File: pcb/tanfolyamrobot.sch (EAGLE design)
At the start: 78 parts, among them IC1 STM32F10XRXT6, IC2 7805, IC4 FT232RL, IC5 LD117AS33TR, M1 DRV8833, Q2 BSS123, Q3 BSS123, Q4 BSS123, X2 PWR, X6 KUSBVX-BS1N

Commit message: small schematic fixes #1
added notes
added component values/types
made RESET and BOOT0 circuit nicer
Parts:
- C10: value (none) -> 22u
- C11: value (none) -> 330n
- C12: value (none) -> 100n
- C13: value 1u -> 100n
- C14: value 2u2 -> 10u
- C16: value (none) -> 68u
- C17: value 22n? -> 22n
- C5, C6: value ? -> 15p
- D7: value (none) -> BAS85
- Q1: value (none) -> 16MHz
- R20, R21: value (none) -> 10K
- R22, R23: value (none) -> 20K
- R24, R25: value (none) -> 4K7
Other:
- note added: "Button's pin is pulled up internally"
- note added: "Check if backlight resistor is required for the used module"
- note added: "Solder jumpers for connecting FTDI output pins to the RESET and BOOT0 circuitry"
- note removed: "TODO: Backlight LED resistor value"
- note removed: "TODO: values, XTAL package"
- moved on the sheet: C10, C11, C12, C13, C14, C17, D3, D4, D5, D6, IC1RESET, JP10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

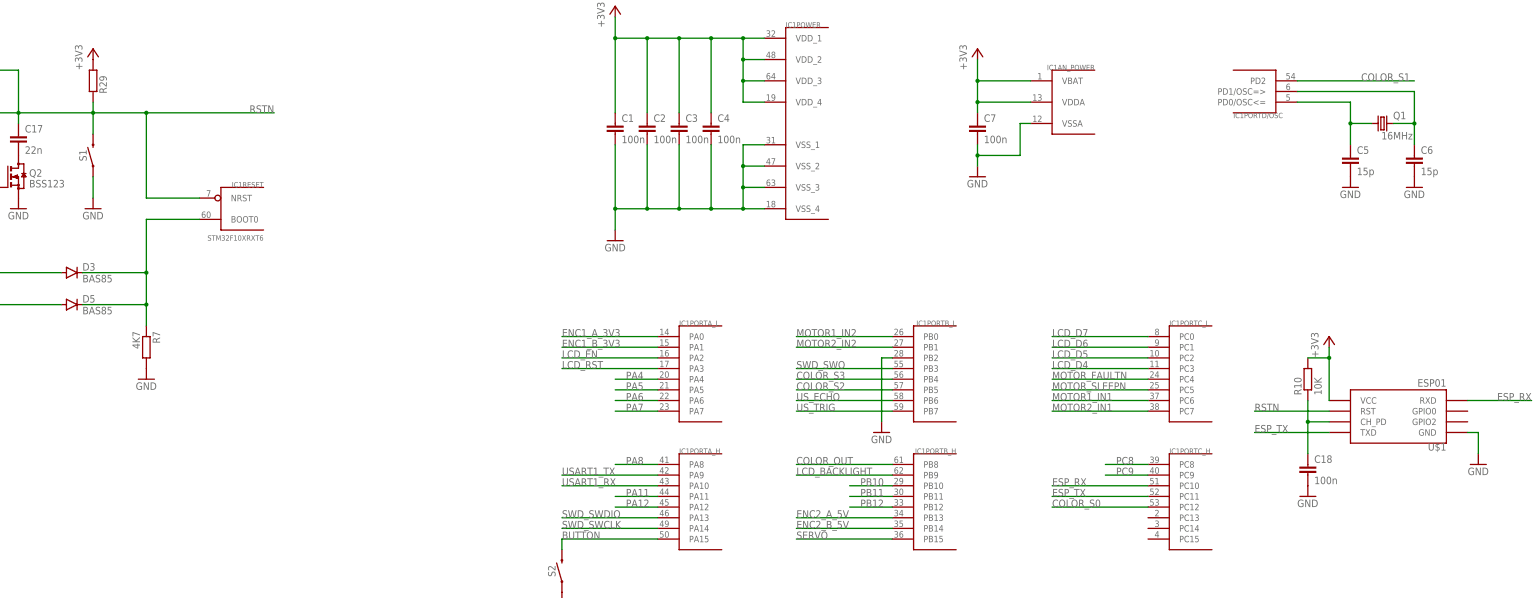
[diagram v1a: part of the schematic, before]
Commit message: added 100n cap to NRST (#1)
and also added ESP reset description
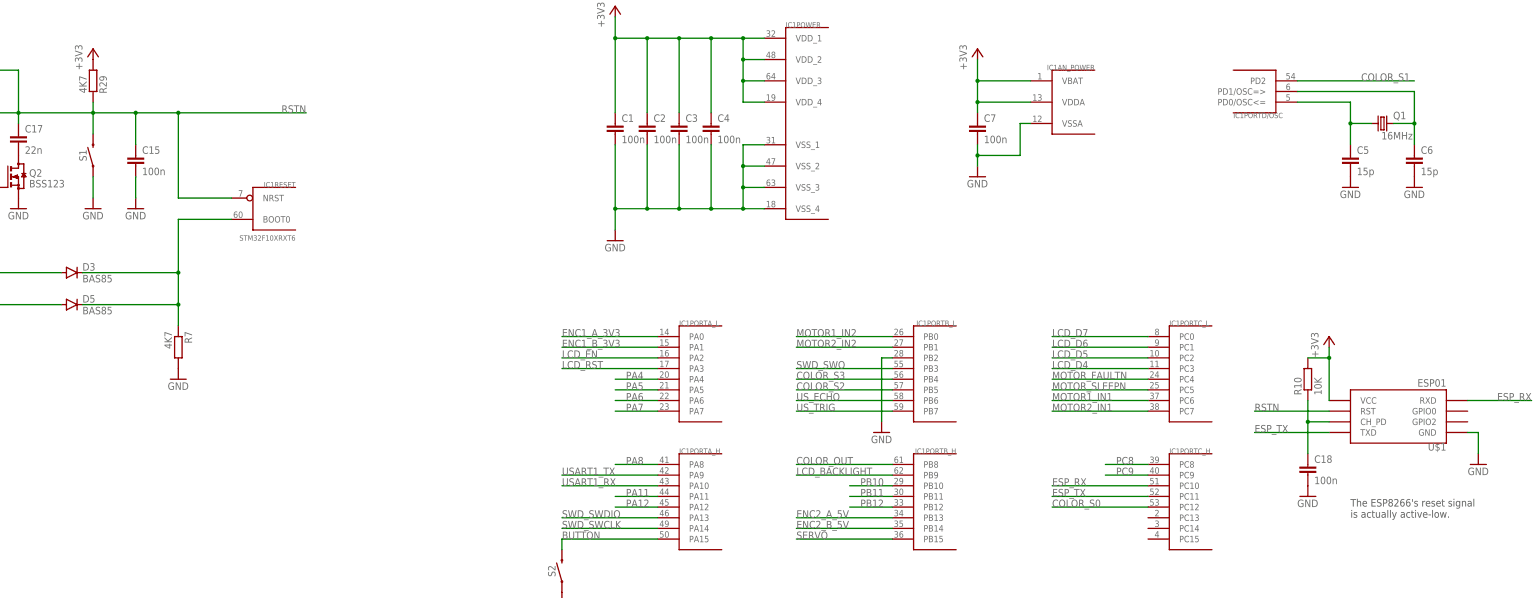
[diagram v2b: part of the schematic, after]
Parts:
- added C15: 100n, rcl:C-EUC0603
- R29: value (none) -> 4K7
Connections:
- net GND: now also C15.2
- net RSTN: now also C15.1
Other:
- note added: "The ESP8266's reset signal is actually active-low."
- moved on the sheet: IC1RESET, R7
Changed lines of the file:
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@@
 <part name="X6" library="con-kycon" library_urn="urn:adsk.eagle:library:157" deviceset="KUSBVX-BS1N" device="" package3d_urn="urn:adsk.eagle:package:7681/1"/>
 <part name="P+9" library="supply1" library_urn="urn:adsk.eagle:library:371" deviceset="+5V" device=""/>
-<part name="R29" library="rcl" library_urn="urn:adsk.eagle:library:334" deviceset="R-EU_" device="R0603" package3d_urn="urn:adsk.eagle:package:23555/3"/>
+<part name="R29" library="rcl" library_urn="urn:adsk.eagle:library:334" deviceset="R-EU_" device="R0603" package3d_urn="urn:adsk.eagle:package:23555/3" value="4K7"/>
 <part name="+3V11" library="supply1" library_urn="urn:adsk.eagle:library:371" deviceset="+3V3" device=""/>
 <part name="D3" library="diode" library_urn="urn:adsk.eagle:library:210" deviceset="DIODE-" device="MICROMELF-W" package3d_urn="urn:adsk.eagle:package:43441/2" value="BAS85"/>
@@
 <part name="GND31" library="supply1" library_urn="urn:adsk.eagle:library:371" deviceset="GND" device=""/>
 <part name="GND32" library="supply1" library_urn="urn:adsk.eagle:library:371" deviceset="GND" device=""/>
+<part name="C15" library="rcl" library_urn="urn:adsk.eagle:library:334" deviceset="C-EU" device="C0603" package3d_urn="urn:adsk.eagle:package:23616/2" value="100n"/>
+<part name="GND33" library="supply1" library_urn="urn:adsk.eagle:library:371" deviceset="GND" device=""/>
 </parts>
 <sheets>
@@
 <text x="429.26" y="83.82" size="1.778" layer="150">Check if backlight resistor is
 required for the used module</text>
+<text x="480.06" y="228.6" size="1.778" layer="97">The ESP8266's reset signal
+is actually active-low.</text>
 </plain>
 <instances>
@@
 <attribute name="NAME" x="419.1" y="335.28" size="1.27" layer="95" rot="MR0"/>
 </instance>
-<instance part="IC1" gate="RESET" x="215.9" y="302.26" smashed="yes" rot="MR0">
-<attribute name="VALUE" x="220.98" y="294.64" size="1.27" layer="95" rot="MR0"/>
-<attribute name="NAME" x="220.98" y="307.34" size="1.27" layer="95" rot="MR0"/>
+<instance part="IC1" gate="RESET" x="223.52" y="302.26" smashed="yes" rot="MR0">
+<attribute name="VALUE" x="228.6" y="294.64" size="1.27" layer="95" rot="MR0"/>
+<attribute name="NAME" x="228.6" y="307.34" size="1.27" layer="95" rot="MR0"/>
 </instance>
 <instance part="+3V1" gate="G$1" x="304.8" y="350.52" smashed="yes">
@@
 <attribute name="VALUE" x="477.52" y="91.44" size="1.778" layer="96"/>
 </instance>
-<instance part="R7" gate="G$1" x="193.04" y="269.24" smashed="yes" rot="R270">
-<attribute name="NAME" x="194.5386" y="273.05" size="1.778" layer="95" rot="R270"/>
-<attribute name="VALUE" x="189.738" y="273.05" size="1.778" layer="96" rot="R270"/>
-</instance>
-<instance part="GND24" gate="1" x="193.04" y="261.62" smashed="yes">
-<attribute name="VALUE" x="190.5" y="259.08" size="1.778" layer="96"/>
+<instance part="R7" gate="G$1" x="200.66" y="269.24" smashed="yes" rot="R270">
+<attribute name="NAME" x="202.1586" y="273.05" size="1.778" layer="95" rot="R270"/>
+<attribute name="VALUE" x="197.358" y="273.05" size="1.778" layer="96" rot="R270"/>
+</instance>
+<instance part="GND24" gate="1" x="200.66" y="261.62" smashed="yes">
+<attribute name="VALUE" x="198.12" y="259.08" size="1.778" layer="96"/>
 </instance>
 <instance part="D5" gate="G$1" x="175.26" y="279.4" smashed="yes">
@@
 <instance part="R29" gate="G$1" x="180.34" y="332.74" smashed="yes" rot="R270">
 <attribute name="NAME" x="181.8386" y="334.01" size="1.778" layer="95" rot="R270"/>
-<attribute name="VALUE" x="177.038" y="336.55" size="1.778" layer="96" rot="R270"/>
+<attribute name="VALUE" x="177.038" y="334.01" size="1.778" layer="96" rot="R270"/>
 </instance>
 <instance part="+3V11" gate="G$1" x="180.34" y="340.36" smashed="yes">
@@
 <instance part="GND32" gate="1" x="474.98" y="81.28" smashed="yes">
 <attribute name="VALUE" x="472.44" y="78.74" size="1.778" layer="96"/>
+</instance>
+<instance part="C15" gate="G$1" x="190.5" y="314.96" smashed="yes">
+<attribute name="NAME" x="192.024" y="315.341" size="1.778" layer="95"/>
+<attribute name="VALUE" x="192.024" y="310.261" size="1.778" layer="96"/>
+</instance>
+<instance part="GND33" gate="1" x="190.5" y="302.26" smashed="yes">
+<attribute name="VALUE" x="187.96" y="299.72" size="1.778" layer="96"/>
 </instance>
 </instances>
@@
 <pinref part="GND31" gate="1" pin="GND"/>
 </segment>
+<segment>
+<pinref part="C15" gate="G$1" pin="2"/>
+<pinref part="GND33" gate="1" pin="GND"/>
+<wire x1="190.5" y1="304.8" x2="190.5" y2="309.88" width="0.1524" layer="91"/>
+</segment>
 </net>
 <net name="+3V3" class="0">
@@
 <wire x1="154.94" y1="325.12" x2="162.56" y2="325.12" width="0.1524" layer="91"/>
 <wire x1="162.56" y1="325.12" x2="180.34" y2="325.12" width="0.1524" layer="91"/>
-<wire x1="180.34" y1="325.12" x2="193.04" y2="325.12" width="0.1524" layer="91"/>
-<wire x1="193.04" y1="325.12" x2="193.04" y2="304.8" width="0.1524" layer="91"/>
-<wire x1="193.04" y1="304.8" x2="205.74" y2="304.8" width="0.1524" layer="91"/>
+<wire x1="180.34" y1="325.12" x2="190.5" y2="325.12" width="0.1524" layer="91"/>
+<wire x1="190.5" y1="325.12" x2="200.66" y2="325.12" width="0.1524" layer="91"/>
+<wire x1="200.66" y1="325.12" x2="200.66" y2="304.8" width="0.1524" layer="91"/>
+<wire x1="200.66" y1="304.8" x2="213.36" y2="304.8" width="0.1524" layer="91"/>
 <pinref part="S1" gate="G$1" pin="2"/>
 <wire x1="180.34" y1="320.04" x2="180.34" y2="325.12" width="0.1524" layer="91"/>
@@
 <wire x1="162.56" y1="335.28" x2="162.56" y2="325.12" width="0.1524" layer="91"/>
 <pinref part="D6" gate="G$1" pin="A"/>
-<wire x1="193.04" y1="325.12" x2="223.52" y2="325.12" width="0.1524" layer="91"/>
-<junction x="193.04" y="325.12"/>
-<label x="223.52" y="325.12" size="1.778" layer="95" rot="MR0"/>
+<wire x1="200.66" y1="325.12" x2="231.14" y2="325.12" width="0.1524" layer="91"/>
+<junction x="200.66" y="325.12"/>
+<label x="231.14" y="325.12" size="1.778" layer="95" rot="MR0"/>
+<pinref part="C15" gate="G$1" pin="1"/>
+<wire x1="190.5" y1="317.5" x2="190.5" y2="325.12" width="0.1524" layer="91"/>
+<junction x="190.5" y="325.12"/>
 </segment>
 <segment>
@@
 <segment>
 <pinref part="IC1" gate="RESET" pin="BOOT0"/>
-<wire x1="205.74" y1="299.72" x2="193.04" y2="299.72" width="0.1524" layer="91"/>
-<wire x1="193.04" y1="299.72" x2="193.04" y2="287.02" width="0.1524" layer="91"/>
+<wire x1="213.36" y1="299.72" x2="200.66" y2="299.72" width="0.1524" layer="91"/>
+<wire x1="200.66" y1="299.72" x2="200.66" y2="287.02" width="0.1524" layer="91"/>
 <pinref part="R7" gate="G$1" pin="1"/>
-<wire x1="193.04" y1="287.02" x2="193.04" y2="279.4" width="0.1524" layer="91"/>
-<wire x1="193.04" y1="274.32" x2="193.04" y2="279.4" width="0.1524" layer="91"/>
-<junction x="193.04" y="279.4"/>
-<wire x1="177.8" y1="279.4" x2="193.04" y2="279.4" width="0.1524" layer="91"/>
+<wire x1="200.66" y1="287.02" x2="200.66" y2="279.4" width="0.1524" layer="91"/>
+<wire x1="200.66" y1="274.32" x2="200.66" y2="279.4" width="0.1524" layer="91"/>
+<junction x="200.66" y="279.4"/>
+<wire x1="177.8" y1="279.4" x2="200.66" y2="279.4" width="0.1524" layer="91"/>
 <pinref part="D5" gate="G$1" pin="C"/>
 <pinref part="D3" gate="G$1" pin="C"/>
-<wire x1="177.8" y1="287.02" x2="193.04" y2="287.02" width="0.1524" layer="91"/>
-<junction x="193.04" y="287.02"/>
-</segment>
-</net>
+<wire x1="177.8" y1="287.02" x2="200.66" y2="287.02" width="0.1524" layer="91"/>
+<junction x="200.66" y="287.02"/>
+</segment>
+</net>
